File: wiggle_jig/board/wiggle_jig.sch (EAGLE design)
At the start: 11 parts, among them IC2 7805TV

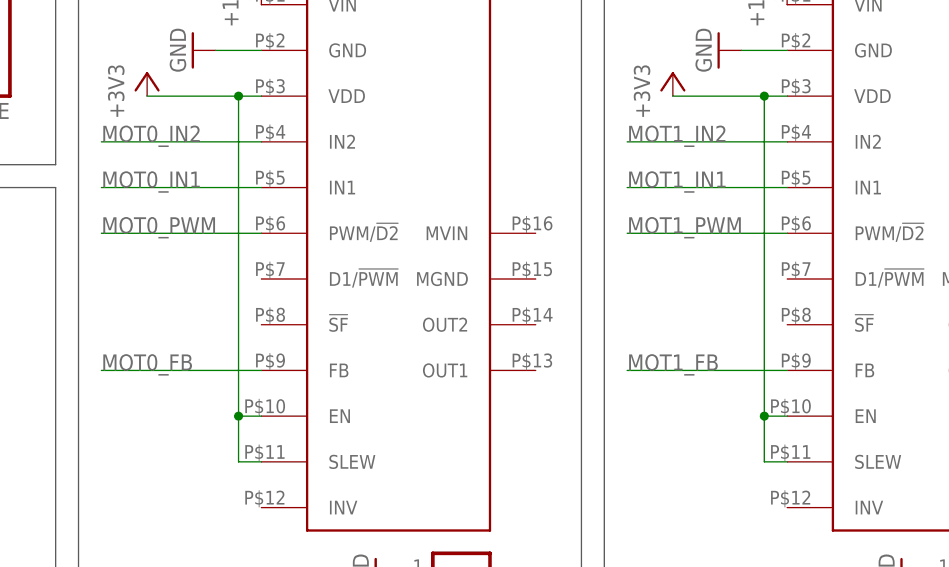
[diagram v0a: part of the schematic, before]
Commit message: First pass at Othermilled laser scanner board. About to update for Bay Area Circuits order.
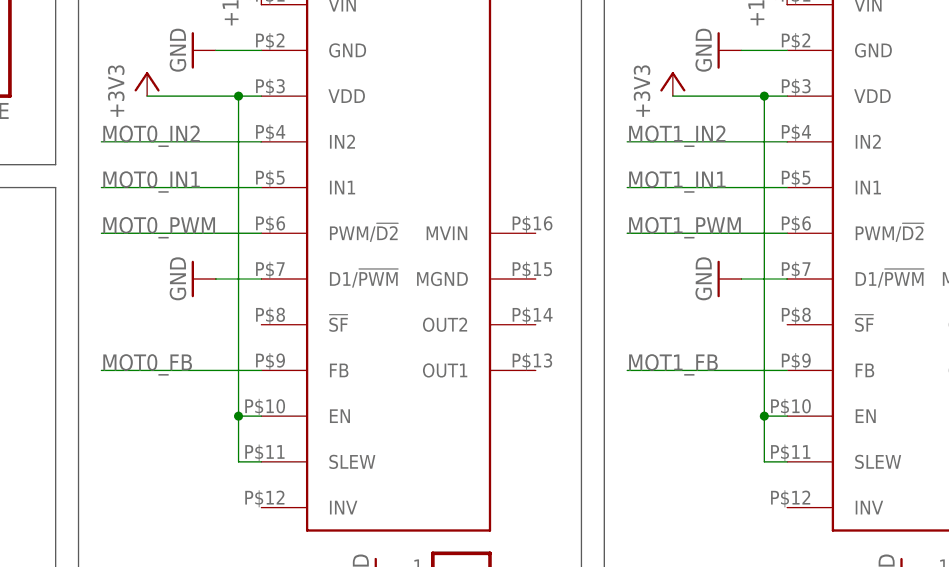
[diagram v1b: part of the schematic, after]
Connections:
- net GND: now also MOT0.D1/!PWM, MOT1.D1/!PWM
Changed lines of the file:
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@@
 <setting verticaltext="up"/>
 </settings>
-<grid distance="0.1" unitdist="inch" unit="inch" style="lines" multiple="1" display="yes" altdistance="0.01" altunitdist="inch" altunit="inch"/>
+<grid distance="0.1" unitdist="inch" unit="inch" style="lines" multiple="1" display="no" altdistance="0.01" altunitdist="inch" altunit="inch"/>
 <layers>
 <layer number="1" name="Top" color="4" fill="1" visible="no" active="no"/>
@@
 <attribute name="REVISION" value="r0.0"/>
 </part>
+<part name="GND4" library="supply1" deviceset="GND" device=""/>
+<part name="GND5" library="supply1" deviceset="GND" device=""/>
 </parts>
 <sheets>
@@
 <attribute name="REVISION" x="2.54" y="93.98" size="1.778" layer="96" display="off"/>
 </instance>
+<instance part="GND4" gate="1" x="205.74" y="68.58" rot="R270"/>
+<instance part="GND5" gate="1" x="147.32" y="68.58" rot="R270"/>
 </instances>
 <busses>
@@
 <pinref part="GND9" gate="1" pin="GND"/>
 </segment>
+<segment>
+<pinref part="MOT1" gate="G$1" pin="D1/!PWM"/>
+<pinref part="GND4" gate="1" pin="GND"/>
+<wire x1="208.28" y1="68.58" x2="213.36" y2="68.58" width="0.1524" layer="91"/>
+</segment>
+<segment>
+<pinref part="MOT0" gate="G$1" pin="D1/!PWM"/>
+<pinref part="GND5" gate="1" pin="GND"/>
+<wire x1="149.86" y1="68.58" x2="154.94" y2="68.58" width="0.1524" layer="91"/>
+</segment>
 </net>
